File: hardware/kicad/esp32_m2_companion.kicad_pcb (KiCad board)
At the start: 6 copper layers, 22 x 42 mm, 59 parts, among them J1 M2_KEYB_2242_EDGE, J3 Conn_01x04, J4 Conn_01x08, Q1 SSM6N56FE, Q2 SSM6N56FE, Q3 SSM6N56FE, U1 USBLC6-2SC6, U2 ESP32-S3-WROOM-1, U3 TMUX1511_RSV, U4 TMUX1511_RSV, U5 TMUX1511_RSV, U6 TPS259470A_RPW

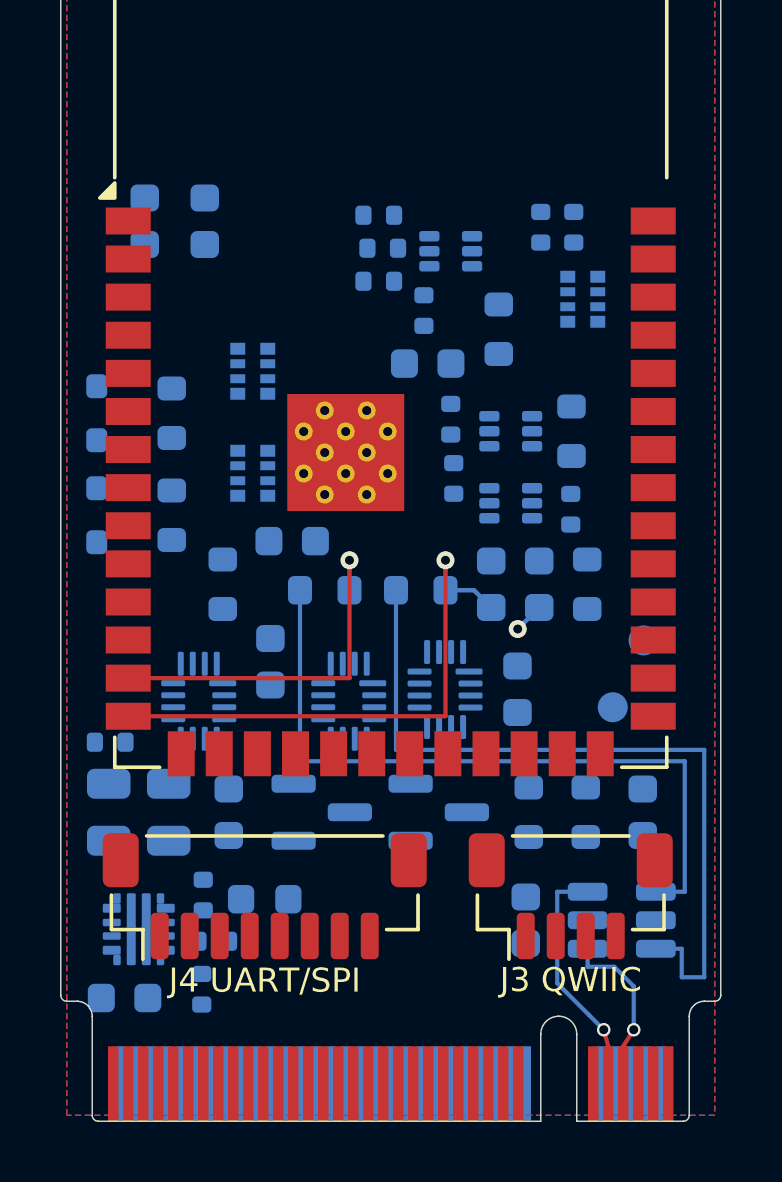
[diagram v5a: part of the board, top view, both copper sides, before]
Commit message: v2 GATE V3 (wip): router pass 2 - 44/70 nets, power fan-out 62/64, 0 clearance errors
tools/v2_route.py (from the v2 probe's grid router): power fan-out to the
In1/In4 planes (via-in-pad when legal), wide +3V3_M2/+3V3_EFUSE at 0.5 mm
with neck-down near pads, then nets by priority (power, EXP chain, rest),
on F/In2/In3/B. KiCad DRC: no clearance/short errors; remaining: 26
unrouted nets, 3 same-net hole-to-hole, C14 edge clearance. Pass 1 (no
neck-down, span order) routed 40/70; pass 2 = tool fix, not a DRC chase.
CLAUDE.md: v2 6-layer rule.

Co-Authored-By: Claude Opus 5.5 <noreply@anthropic.com>
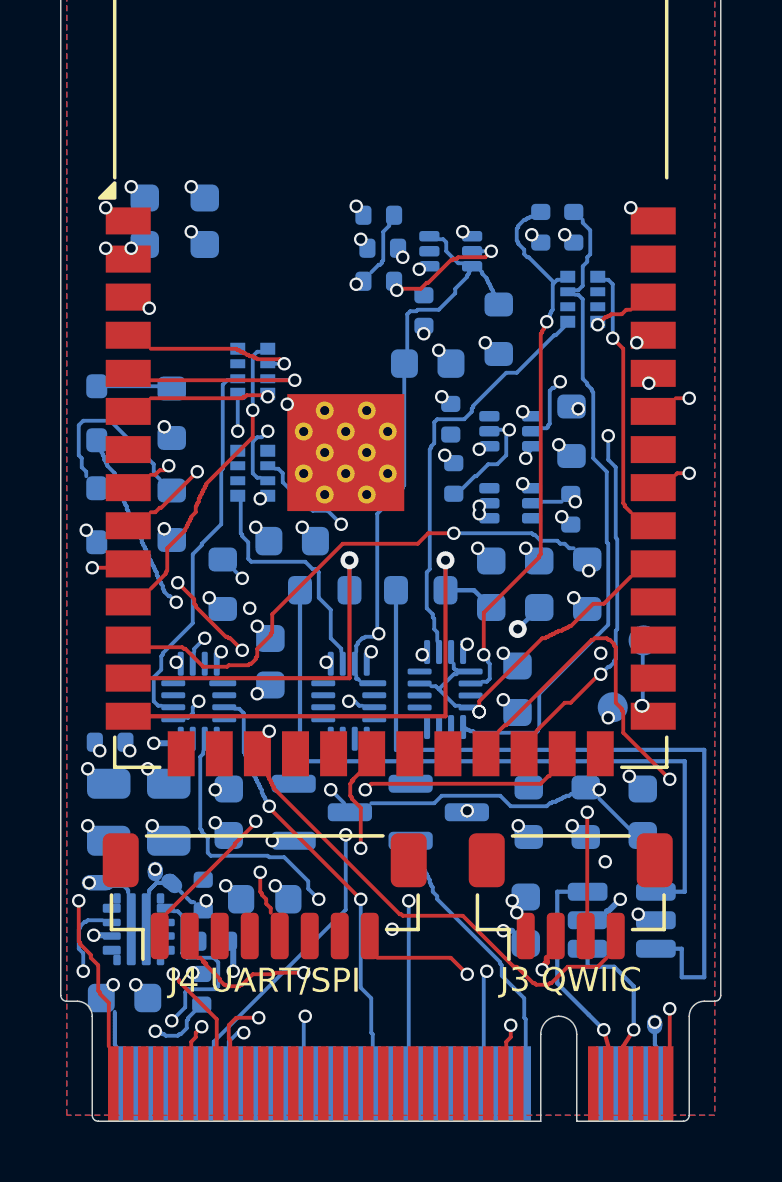
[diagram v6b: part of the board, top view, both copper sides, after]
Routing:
- net CONFIG_2: track 0.00 -> 32.0 mm, vias 0 -> 2
- net +3V3_M2: track 0.00 -> 30.8 mm, vias 0 -> 5
- net EXP_OE: track 0.00 -> 30.5 mm, vias 0 -> 3
- net EN: track 0.00 -> 30.3 mm, vias 0 -> 6
- net CONFIG_3: track 0.00 -> 30.0 mm, vias 0 -> 3
- net RXD0: track 0.00 -> 28.7 mm, vias 0 -> 2
- net IO8: track 0.00 -> 28.5 mm, vias 0 -> 3
- net TXD0: track 0.00 -> 25.8 mm, vias 0 -> 2
- net IO21: track 0.00 -> 24.2 mm, vias 0 -> 2
- net LED_STATUS_n: track 0.00 -> 23.5 mm, vias 0 -> 3
- net WAKE_ON_WWAN_n: track 0.00 -> 23.4 mm, vias 0 -> 3
- net EXP_1_S: track 0.00 -> 21.2 mm
- net W_DISABLE2_n: track 0.00 -> 20.9 mm, vias 0 -> 3
- net IO9: track 0.00 -> 20.6 mm, vias 0 -> 2
- net EXP_0_S: track 0.00 -> 17.8 mm, vias 0 -> 2
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
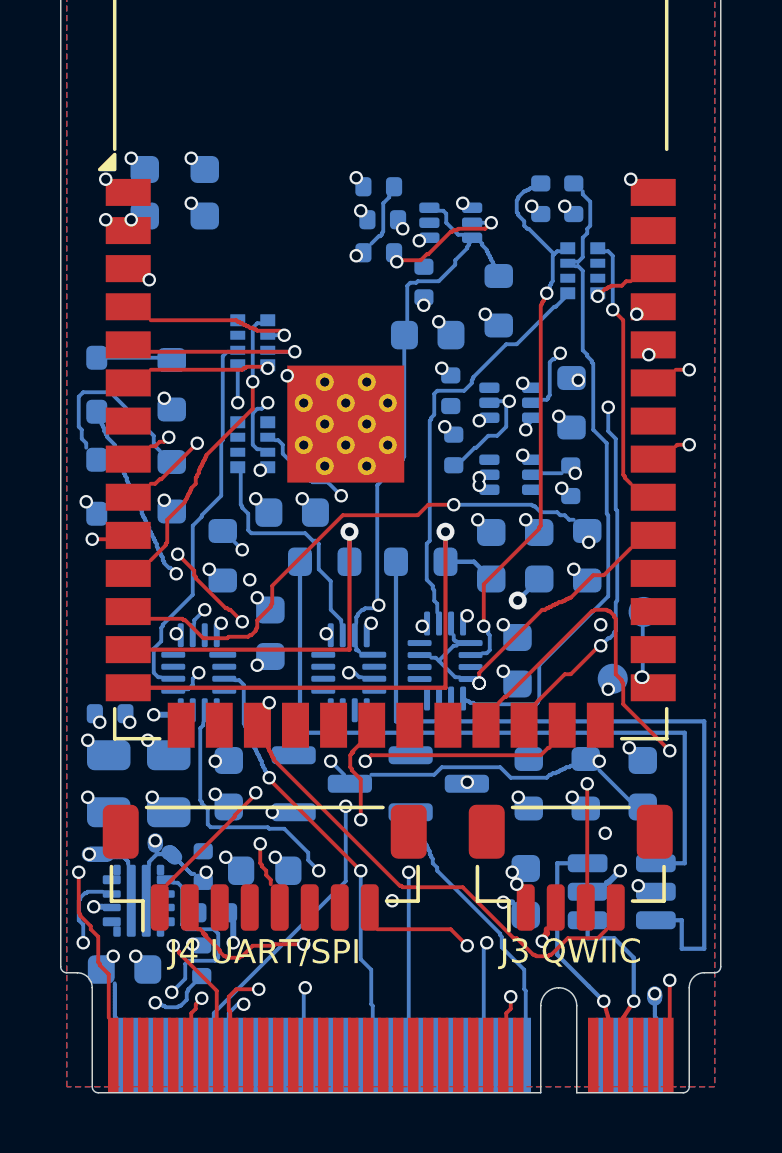
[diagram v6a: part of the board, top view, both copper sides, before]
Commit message: v2 GATE V3 (wip): USB rerouted via In2/F, 6 provisions removed (owner), escape fan-out
- Schematic: R5/R6 (DNP I2C pull-ups), C8/C9 (DNP USB SI shunts), R7/R8
  (0R USB links) removed - owner decision; U1 connects straight to the
  module. ERC + contract check PASS; review PDF/BOM refreshed.
- tools/v2_usb_route.py: scripted, locked USB route U1 -> In2 (on L2 GND)
  -> F.Cu -> module pads 13/14; skew 5.2 mm.
- Switches + caps re-placed with escape room; router gains escape fan-out,
  --fanout-missing, --short-first, sense-branch thinning, neck-down,
  via-hole map; helpers: ripnets, clear_conflicts, drop_dup_vias,
  drop_dangling, nudge, zoom.
- State: 18 nets still open (EXP/switch cluster + LED_1#); no clearance
  errors in routed copper.

Co-Authored-By: Claude Opus 5.5 <noreply@anthropic.com>
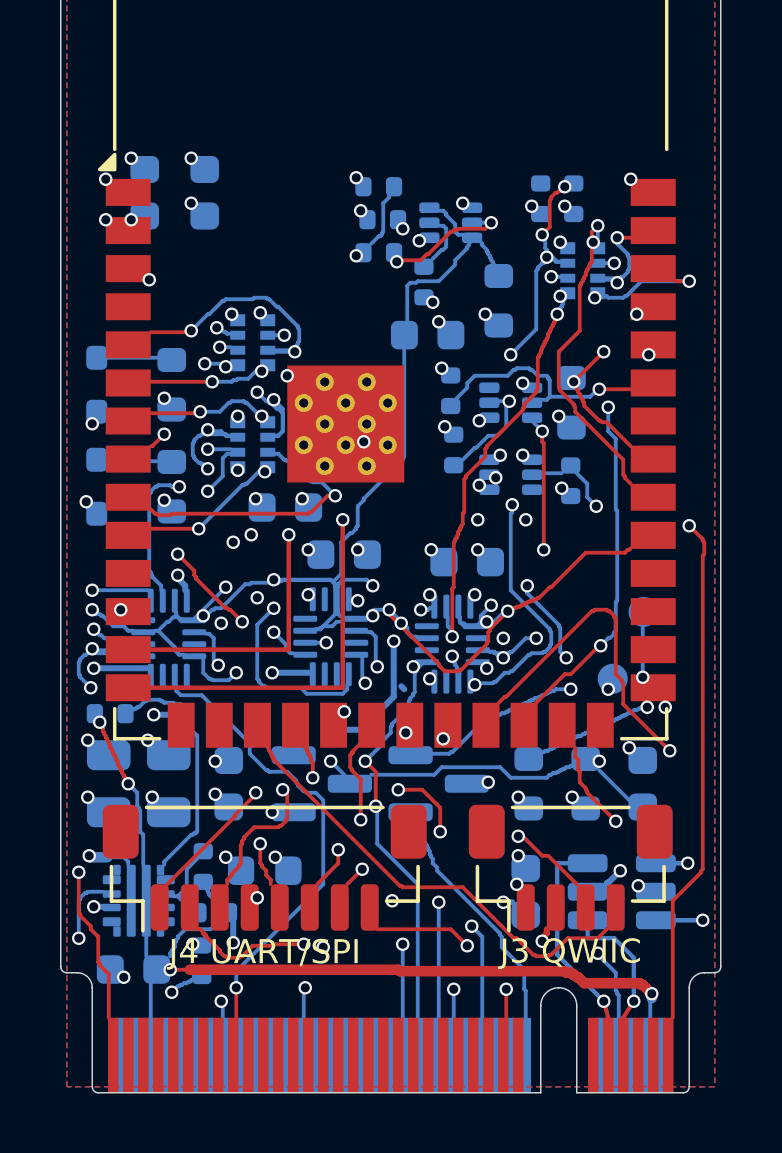
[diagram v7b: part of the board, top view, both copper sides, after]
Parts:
- removed C8, C9: SI-tune, Capacitor_SMD:C_0603_1608Metric
- removed R5, R6: 10k, Resistor_SMD:R_0603_1608Metric
- removed R7, R8: 0R, Resistor_SMD:R_0603_1608Metric
- moved C11 4.22 mm to (96.5, 130.5), turned to 180 degrees
- moved C10 3.69 mm to (102.5, 132.3), turned to 180 degrees
- moved C12 2.23 mm to (98.4, 132.1)
- moved U4 1.52 mm to (92.6, 134.9)
- moved U5 1.34 mm to (98.0, 134.8)
- moved U3 0.61 mm to (102.1, 135.0)
- moved C14 0.30 mm to (91.4, 145.9), turned to 180 degrees
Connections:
- U1 pad 4: USB_D_N_ESD -> USB_D_N
- U1 pad 6: USB_D_P_ESD -> USB_D_P
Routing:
- net USB_D_P_ESD: track 25.7 -> 0.00 mm
- net USB_D_N_ESD: track 23.8 -> 0.00 mm
- net EXP_OE: track 30.5 -> 52.8 mm, vias 3 -> 14
- net USB_D_P: track 18.5 -> 39.7 mm, vias 1 -> 2
- net EXP_0_S: track 17.8 -> 0.00 mm, vias 2 -> 1
- net W_DISABLE1_n: track 0.00 -> 17.1 mm, vias 0 -> 2
- net EXP_0: track 0.00 -> 16.1 mm, vias 0 -> 3
- net EXP_9_S: track 0.00 -> 15.5 mm, vias 0 -> 3
- net EXP_11: track 14.7 -> 0.05 mm, vias 2 -> 1
- net USB_D_N: track 19.9 -> 34.5 mm
- net EXP_8: track 13.9 -> 0.00 mm, vias 2 -> 0
- net EXP_2: track 0.00 -> 13.5 mm, vias 0 -> 3
- net EXP_4: track 13.2 -> 0.00 mm, vias 2 -> 0
- net EXP_1: track 0.00 -> 12.9 mm, vias 0 -> 2
- net EXP_7: track 13.5 -> 1.90 mm, vias 2 -> 1
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
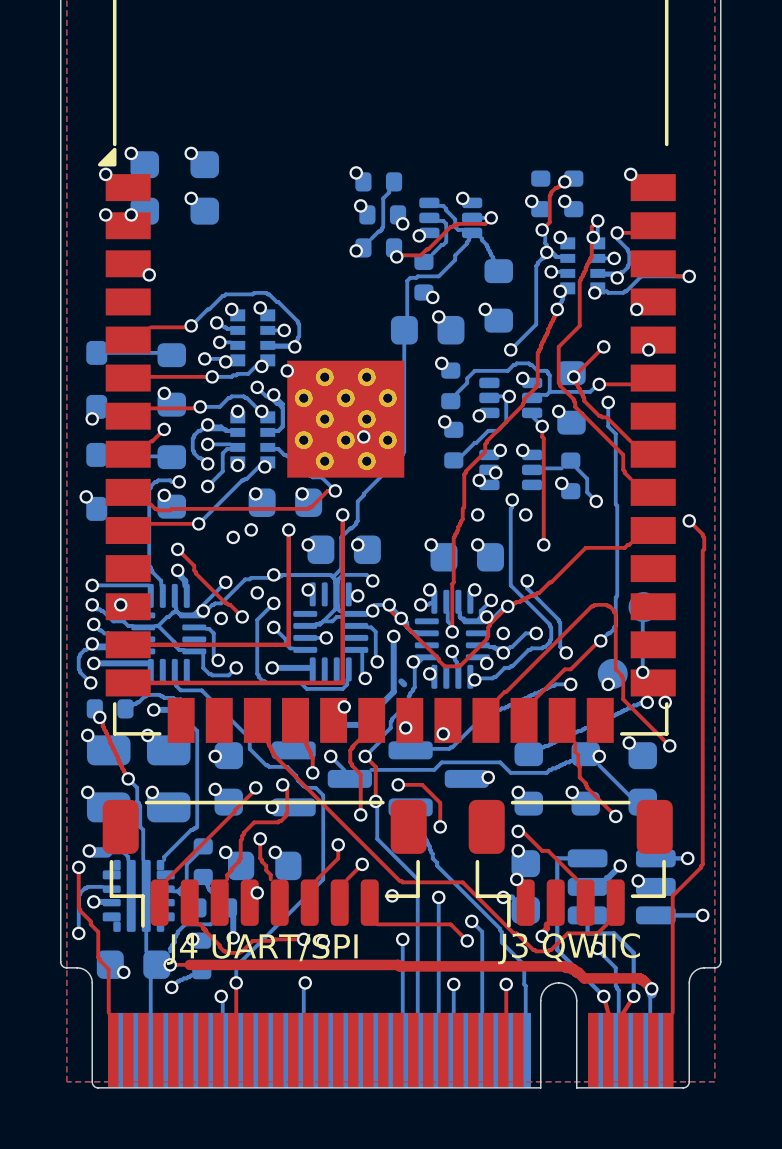
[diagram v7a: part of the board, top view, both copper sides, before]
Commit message: v2 GATE V3 (wip): TI RSV land pattern, RN2/RN3 flipped, 15 nets left
- tools/gen_fp_rsv.py: TMUX1511 footprint from TI's RSV0016A land pattern
  (tmux1511.pdf p.37), pads 0.15 mm shorter than KiCad stock.
- RN2/RN3 rotated 180 deg (MCU side now faces the module IO pads).
- tools/v2_drop_orphan_fanout.py: remove plane fan-out no longer anchored
  to a pad; v2_drop_dangling --planes-only.
- Open: switch pin escapes (~4 pins/switch), RN1 inner pads, LED_1_n.

Co-Authored-By: Claude Opus 5.5 <noreply@anthropic.com>
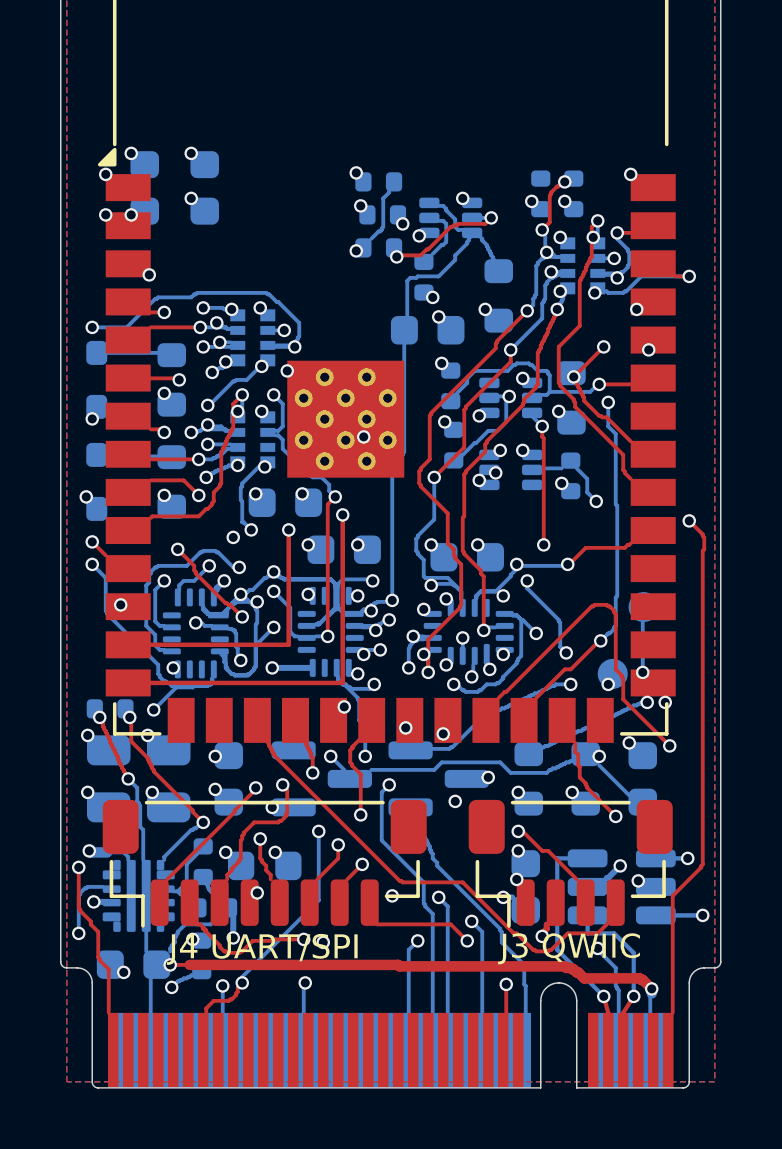
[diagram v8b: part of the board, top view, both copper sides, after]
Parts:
- U3, U4, U5: footprint Package_DFN_QFN:UQFN-16_1.8x2.6mm_P0.4mm -> esp32_m2_companion:TI_RSV0016A_UQFN-16_1.8x2.6mm_P0.4mm
- moved U4 0.90 mm to (93.5, 134.9)
- moved U3 0.60 mm to (102.6, 134.8), turned to 90 degrees
- turned RN2 to 0 degrees
- turned RN3 to 0 degrees
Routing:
- net EXP_5_S: track 0.53 -> 27.4 mm, vias 1 -> 4
- net EXP_6: track 17.2 -> 33.2 mm, vias 3 -> 2
- net EXP_9: track 0.00 -> 15.6 mm, vias 0 -> 4
- net EXP_2_S: track 0.30 -> 15.6 mm, vias 1 -> 4
- net EXP_9_S: track 15.5 -> 0.20 mm, vias 3 -> 1
- net EXP_5: track 15.2 -> 0.00 mm, vias 1 -> 0
- net EXP_2: track 13.5 -> 0.05 mm, vias 3 -> 1
- net EXP_4_S: track 1.27 -> 14.4 mm, vias 2 -> 4
- net IO18: track 0.05 -> 11.5 mm, vias 1 -> 3
- net EXP_7_S: track 9.99 -> 0.05 mm, vias 3 -> 1
- net EXP_8_S: track 1.33 -> 10.1 mm, vias 2 -> 4
- net GND: track 10.5 -> 3.02 mm, vias 40 -> 34
- net IO5: track 7.89 -> 3.20 mm
- net IO15: track 8.01 -> 3.54 mm, vias 3 -> 2
- net IO4: track 0.30 -> 3.51 mm, vias 1 -> 3
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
